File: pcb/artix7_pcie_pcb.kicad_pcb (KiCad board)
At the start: 4 copper layers, 211 parts, among them CON301 BARREL_JACK, J1101 SFP_CONN, J201 PCIe_x1, J801 FX10B-80S/8-SV, J901 JTAG-XILINX-TC, P1201 CONN_02X05, P1202 CONN_02X05, SW1201 SW_PUSH, SW1202 SW_PUSH, SW901 SW_PUSH, U1001 FOX924, U1002 NB3L553, U1003 Si5338C, U301 LTM4622, U302 LTM4622, U303 ADP170, U304 TPS72615, U401 XC7Axxt-FGG484, U501 DDR3-x16, U901 S25FL256SAGNFI

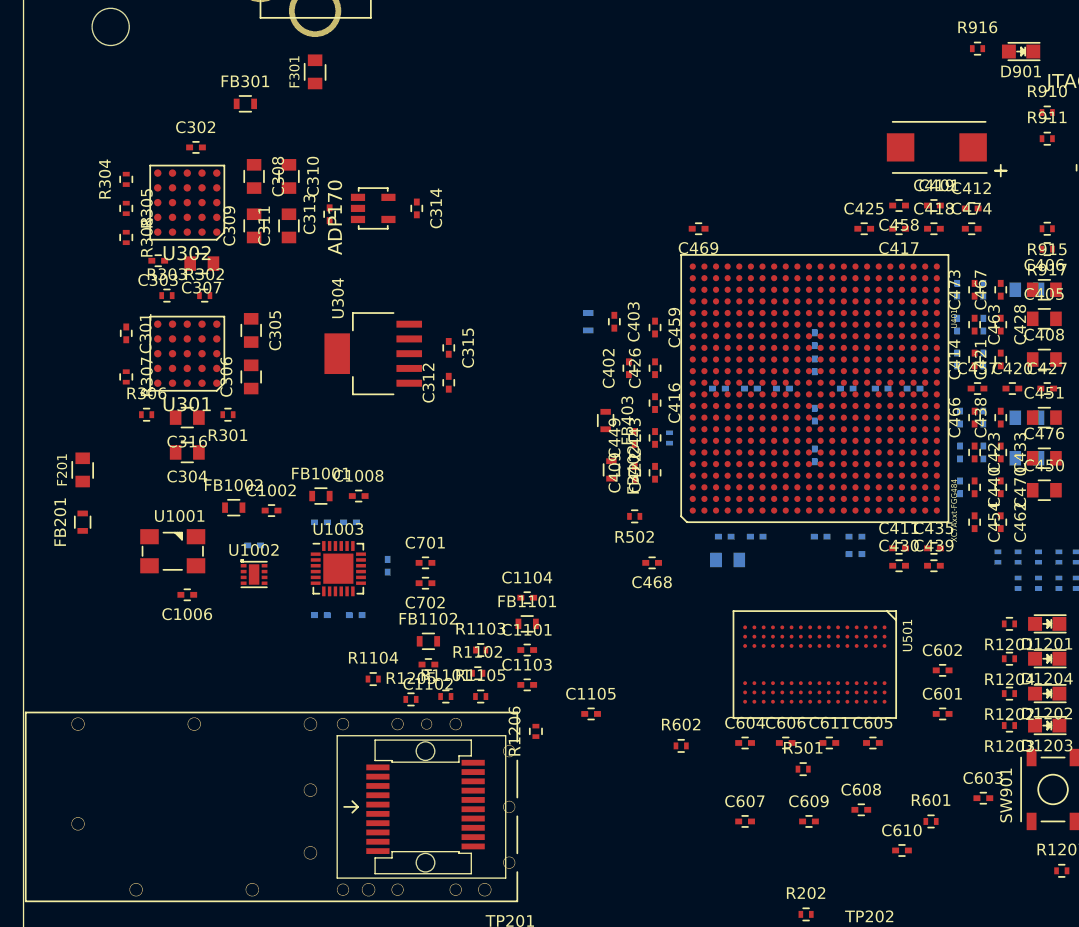
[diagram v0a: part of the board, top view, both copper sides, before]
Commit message: Finished initial component placement
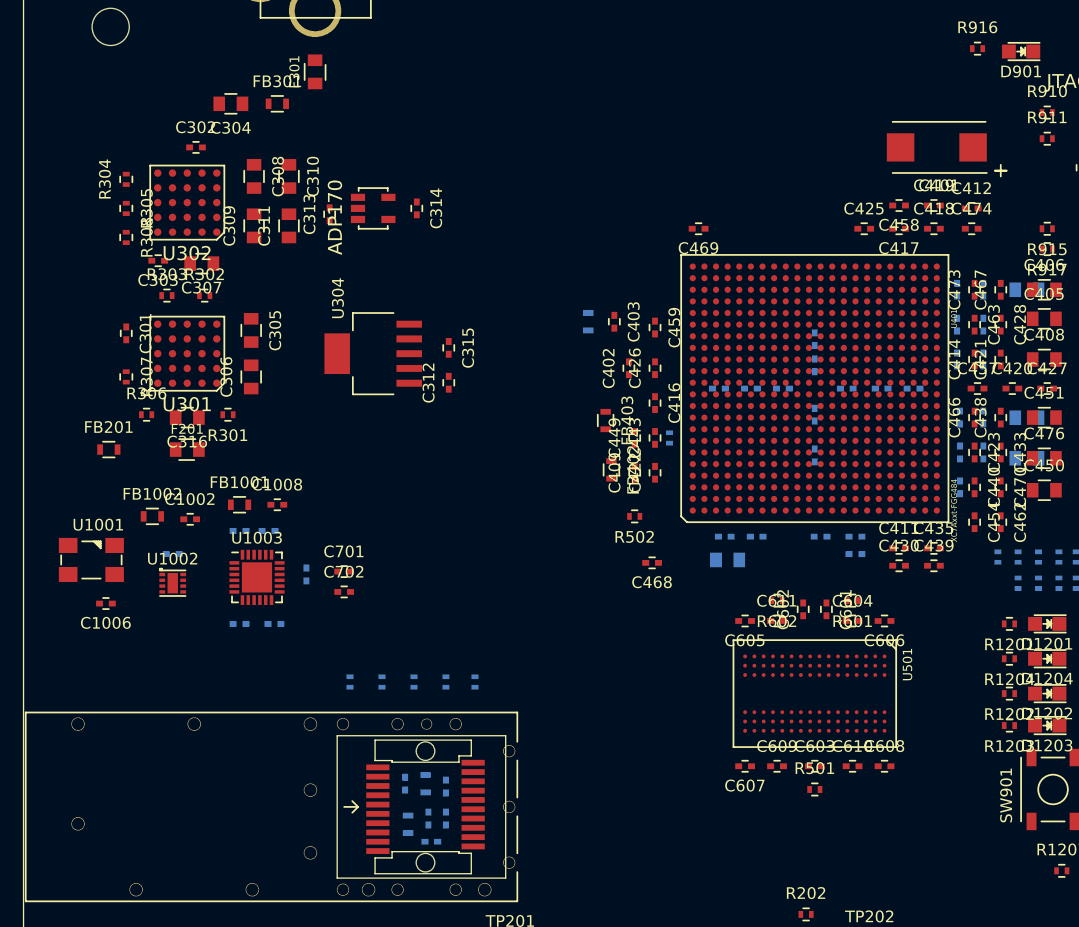
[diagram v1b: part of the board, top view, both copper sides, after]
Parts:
- removed R1205, R1206: R, wbraun_smd:R_0402
- C1101, C1102, C1103, C1104, C1105, FB1101, FB1102, R1101, R1102, R1103, R1104, R1105: moved to B.Cu
- moved C304 30.2 mm to (59.8, 63.0)
- moved C1104 22.6 mm to (77.0, 126.5)
- moved R601 20.2 mm to (113.2, 105.8), turned to 180 degrees
- moved FB1101 20.1 mm to (75.0, 125.0), turned to 90 degrees
- moved C1105 17.1 mm to (74.8, 121.5), turned to 270 degrees
- moved C1101 16.8 mm to (76.8, 124.5), turned to 270 degrees
- moved C605 15.2 mm to (104.0, 107.5), turned to 180 degrees
- moved R602 15.0 mm to (106.8, 105.8), turned to 180 degrees
- moved C603 14.8 mm to (110.0, 120.0)
- moved C604 14.0 mm to (113.2, 107.5)
- moved C606 13.5 mm to (116.0, 107.5), turned to 180 degrees
- moved C1103 13.5 mm to (78.2, 124.5), turned to 270 degrees
- moved C601 13.5 mm to (111.0, 106.5), turned to 270 degrees
- moved C602 13.1 mm to (109.0, 106.5), turned to 90 degrees
- moved FB1102 12.3 mm to (76.5, 121.5), turned to 270 degrees
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
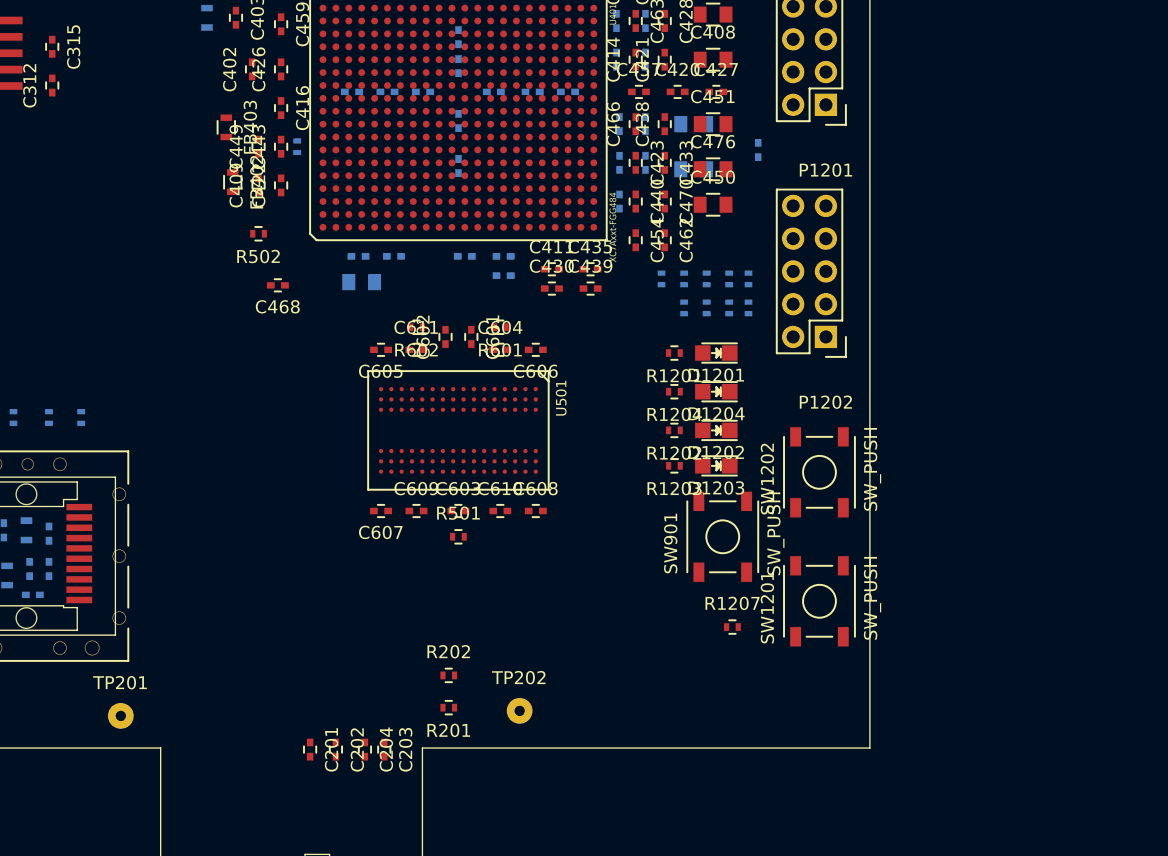
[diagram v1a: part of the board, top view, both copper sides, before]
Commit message: DDR routing test 1
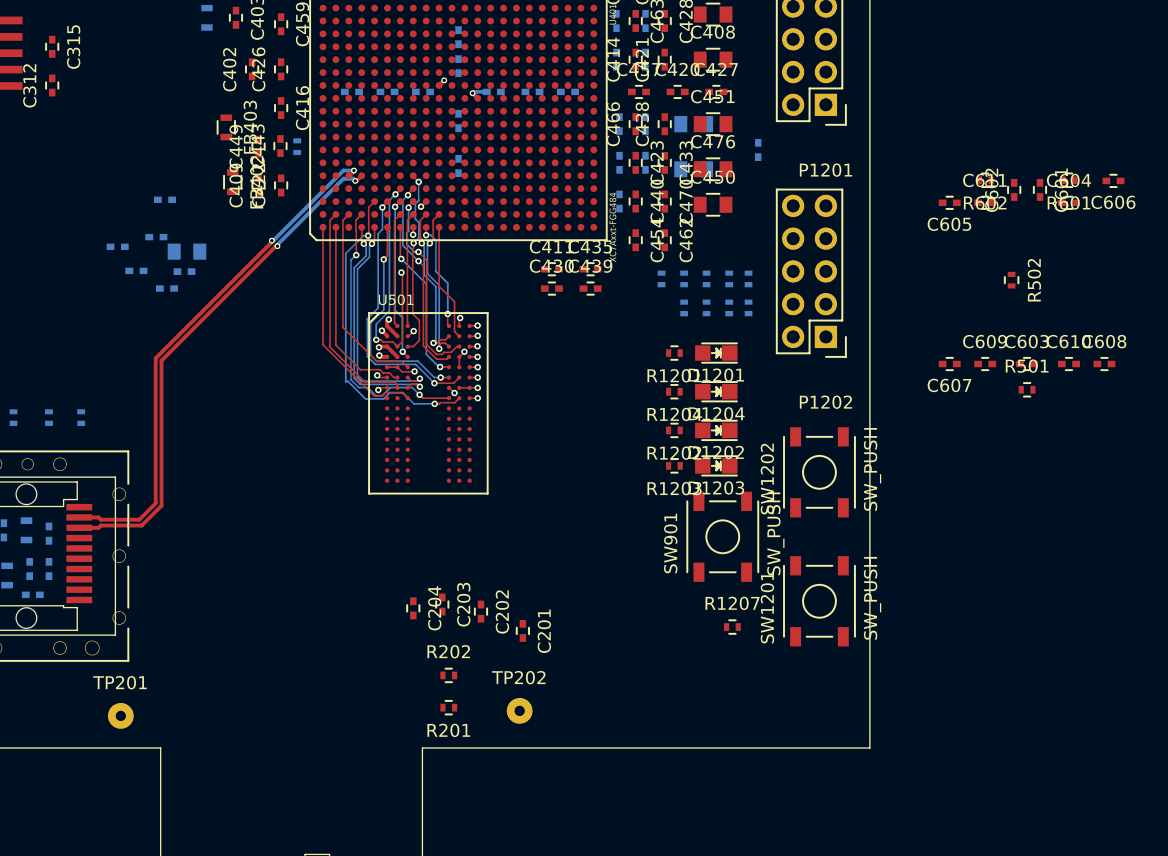
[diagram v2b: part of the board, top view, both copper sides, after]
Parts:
- C468: moved to B.Cu
- moved R502 58.5 mm to (152.9, 102.1), turned to 270 degrees
- moved C606 46.7 mm to (160.8, 94.4)
- moved C601 45.5 mm to (155.1, 95.1)
- moved C602 45.5 mm to (153.1, 95.1)
- moved C603 45.5 mm to (154.1, 108.6)
- moved C604 45.5 mm to (157.3, 96.1)
- moved C605 45.5 mm to (148.1, 96.1)
- moved C607 45.5 mm to (148.1, 108.6)
- moved C608 45.5 mm to (160.1, 108.6)
- moved C609 45.5 mm to (150.8, 108.6)
- moved C610 45.5 mm to (157.3, 108.6)
- moved C611 45.5 mm to (150.8, 96.1)
- moved R501 45.5 mm to (154.1, 110.6)
- moved R601 45.5 mm to (157.3, 94.3)
- moved R602 45.5 mm to (150.8, 94.3)
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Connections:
- U401 pad A1: /DDR3/DDR3_ADDR[11] -> /DDR3/DDR3_DQ[4]
- U401 pad A11: (no net) -> GND
- U401 pad A12: (no net) -> GND
- U401 pad A2: (no net) -> GND
- U401 pad A22: (no net) -> GND
- U401 pad A3: (no net) -> GND
- U401 pad A5: (no net) -> GND
- U401 pad A7: (no net) -> GND
- U401 pad A9: (no net) -> GND
- U401 pad AA12: (no net) -> GND
- U401 pad AA2: (no net) -> GND
- U401 pad AA22: (no net) -> GND
- U401 pad AB19: (no net) -> GND
- U401 pad AB9: (no net) -> GND
- U401 pad B1: /DDR3/DDR3_ADDR[12] -> /DDR3/DDR3_DQ[2]
- U401 pad B12: (no net) -> GND
- U401 pad B19: (no net) -> GND
- U401 pad B2: /DDR3/DDR3_ADDR[9] -> /DDR3/DDR3_DQ[6]
- U401 pad B3: (no net) -> GND
- U401 pad C10: (no net) -> GND
- U401 pad C12: (no net) -> GND
- U401 pad C16: (no net) -> GND
- U401 pad C2: /DDR3/DDR3_ADDR[10] -> /DDR3/DDR3_DQ[0]
- U401 pad C3: (no net) -> GND
- U401 pad C6: (no net) -> GND
- U401 pad D1: /DDR3/DDR3_CK_N -> /DDR3/DDR3_DQS[0]_N
- U401 pad D12: (no net) -> GND
- U401 pad D13: (no net) -> GND
- U401 pad D2: /DDR3/DDR3_ADDR[7] -> /DDR3/DDR3_DQ[7]
- U401 pad D3: (no net) -> GND
- U401 pad D4: (no net) -> GND
- U401 pad D8: (no net) -> GND
- U401 pad E1: /DDR3/DDR3_CK_P -> /DDR3/DDR3_DQS[0]_P
- U401 pad E11: (no net) -> GND
- U401 pad E2: /DDR3/DDR3_ADDR[8] -> Net-(U401-PadE2)
- U401 pad E20: (no net) -> GND
- U401 pad E3: /DDR3/DDR3_ADDR[3] -> /DDR3/DDR3_DQ[5]
- U401 pad E4: (no net) -> GND
- U401 pad E5: (no net) -> GND
- U401 pad E7: (no net) -> GND
- U401 pad E9: (no net) -> GND
- U401 pad F1: /DDR3/DDR3_ADDR[5] -> /DDR3/DDR3_DQ[1]
- U401 pad F11: (no net) -> GND
- U401 pad F17: (no net) -> GND
- U401 pad F3: /DDR3/DDR3_ADDR[4] -> /DDR3/DDR3_DQ[3]
- U401 pad F5: (no net) -> GND
- U401 pad G1: /DDR3/DDR3_ADDR[6] -> /DDR3/DDR3_DM[0]
- U401 pad G10: (no net) -> GND
- U401 pad G12: (no net) -> GND
- U401 pad G14: (no net) -> GND
- U401 pad G2: /DDR3/DDR3_BA[2] -> /DDR3/DDR3_DQ[13]
- U401 pad G3: /DDR3/DDR3_CKE -> /DDR3/DDR3_DM[1]
- U401 pad G4: Net-(U401-PadG4) -> /DDR3/DDR3_DQ[11]
- U401 pad G5: (no net) -> GND
- U401 pad G6: (no net) -> GND
- U401 pad G7: (no net) -> GND
- U401 pad G8: (no net) -> GND
- U401 pad G9: (no net) -> GND
- U401 pad H1: (no net) -> GND
- U401 pad H11: (no net) -> GND
- U401 pad H2: /DDR3/DDR3_ADDR[0] -> /DDR3/DDR3_DQ[15]
- U401 pad H21: (no net) -> GND
- U401 pad H3: /DDR3/DDR3_WE_N -> /DDR3/DDR3_DQ[10]
- U401 pad H4: /DDR3/DDR3_ODT -> /DDR3/DDR3_DQ[8]
- U401 pad H5: /DDR3/DDR3_CAS_N -> /DDR3/DDR3_DQ[9]
- U401 pad H7: (no net) -> GND
- U401 pad H9: (no net) -> GND
- U401 pad J1: /DDR3/DDR3_ADDR[1] -> /DDR3/DDR3_DQ[12]
- U401 pad J10: (no net) -> GND
- U401 pad J12: (no net) -> GND
- U401 pad J18: (no net) -> GND
- U401 pad J2: /DDR3/DDR3_BA[0] -> /DDR3/DDR3_DQS[1]_N
- U401 pad J4: /DDR3/DDR3_DQ[1] -> Net-(U401-PadJ4)
- U401 pad J5: /DDR3/DDR3_RAS_N -> Net-(U401-PadJ5)
- U401 pad J6: /DDR3/DDR3_DQ[6] -> Net-(U401-PadJ6)
- U401 pad J8: (no net) -> GND
- U401 pad K1: /DDR3/DDR3_ADDR[2] -> /DDR3/DDR3_DQ[14]
- U401 pad K11: (no net) -> GND
- U401 pad K15: (no net) -> GND
- U401 pad K2: /DDR3/DDR3_BA[1] -> /DDR3/DDR3_DQS[1]_P
- U401 pad K3: /DDR3/DDR3_DQ[3] -> Net-(U401-PadK3)
- U401 pad K4: /DDR3/DDR3_DQ[0] -> Net-(U401-PadK4)
- U401 pad K5: (no net) -> GND
- U401 pad K6: /DDR3/DDR3_DQ[5] -> Net-(U401-PadK6)
- U401 pad K7: (no net) -> GND
- U401 pad K9: (no net) -> GND
- U401 pad L1: /DDR3/DDR3_DQS[0]_N -> Net-(U401-PadL1)
- U401 pad L2: (no net) -> GND
- U401 pad L22: (no net) -> GND
- U401 pad L3: /DDR3/DDR3_DQ[2] -> Net-(U401-PadL3)
- U401 pad L4: /DDR3/DDR3_RESET_N -> Net-(U401-PadL4)
- U401 pad L5: /DDR3/DDR3_DQ[7] -> Net-(U401-PadL5)
- U401 pad L8: (no net) -> GND
- U401 pad M1: /DDR3/DDR3_DQS[0]_P -> Net-(U401-PadM1)
- U401 pad M11: (no net) -> GND
- U401 pad M19: (no net) -> GND
- U401 pad M2: /DDR3/DDR3_DQ[4] -> Net-(U401-PadM2)
- U401 pad M3: /DDR3/DDR3_DM[0] -> Net-(U401-PadM3)
- U401 pad M5: /DDR3/DDR3_DQ[14] -> Net-(U401-PadM5)
- U401 pad M6: /DDR3/DDR3_DQ[13] -> Net-(U401-PadM6)
- U401 pad M7: (no net) -> GND
- U401 pad N16: (no net) -> GND
- U401 pad N2: /DDR3/DDR3_DQ[12] -> Net-(U401-PadN2)
- U401 pad N3: /DDR3/DDR3_DQ[8] -> Net-(U401-PadN3)
- U401 pad N4: /DDR3/DDR3_DM[1] -> Net-(U401-PadN4)
- U401 pad N6: (no net) -> GND
- U401 pad N8: (no net) -> GND
- U401 pad P1: /DDR3/DDR3_DQ[10] -> Net-(U401-PadP1)
- U401 pad P11: (no net) -> GND
- U401 pad P13: (no net) -> GND
- U401 pad P2: /DDR3/DDR3_DQ[11] -> Net-(U401-PadP2)
- U401 pad P3: (no net) -> GND
- U401 pad P4: /DDR3/DDR3_DQS[1]_N -> Net-(U401-PadP4)
- U401 pad P5: /DDR3/DDR3_DQS[1]_P -> Net-(U401-PadP5)
- U401 pad P6: /DDR3/DDR3_DQ[15] -> Net-(U401-PadP6)
- U401 pad P7: (no net) -> GND
- U401 pad P9: (no net) -> GND
- U401 pad R1: /DDR3/DDR3_DQ[9] -> Net-(U401-PadR1)
- U401 pad R10: (no net) -> GND
- U401 pad R12: (no net) -> GND
- U401 pad R20: (no net) -> GND
- U401 pad R8: (no net) -> GND
- U401 pad T11: (no net) -> GND
- U401 pad T17: (no net) -> GND
- U401 pad T7: (no net) -> GND
- U401 pad T9: (no net) -> GND
- U401 pad U14: (no net) -> GND
- U401 pad U4: (no net) -> GND
- U401 pad V1: (no net) -> GND
- U401 pad V11: (no net) -> GND
- U401 pad V21: (no net) -> GND
- U401 pad W18: (no net) -> GND
- U401 pad W8: (no net) -> GND
- U401 pad Y15: (no net) -> GND
- U401 pad Y5: (no net) -> GND
- U501 pad E9: (no net) -> +1V5
- U501 pad H2: (no net) -> +1V5
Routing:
- net /FPGA Transceivers/SFP_TX_P: track 0.00 -> 40.0 mm, vias 0 -> 2
- net /FPGA Transceivers/SFP_TX_N: track 0.00 -> 39.8 mm, vias 0 -> 2
- net /DDR3/DDR3_DQ[5]: track 0.00 -> 25.2 mm, vias 0 -> 2
- net /DDR3/DDR3_DQ[7]: track 0.00 -> 21.9 mm, vias 0 -> 2
- net /DDR3/DDR3_DQ[3]: track 0.00 -> 20.8 mm, vias 0 -> 2
- net /DDR3/DDR3_DQ[11]: track 0.00 -> 20.3 mm, vias 0 -> 3
- net /DDR3/DDR3_DQS[0]_N: track 0.00 -> 18.7 mm, vias 0 -> 2
- net /DDR3/DDR3_DQS[0]_P: track 0.00 -> 18.3 mm, vias 0 -> 2
- net /DDR3/DDR3_DQ[4]: track 0.00 -> 17.6 mm
- net /DDR3/DDR3_DQ[1]: track 0.00 -> 17.3 mm, vias 0 -> 2
- net /DDR3/DDR3_DQ[6]: track 0.00 -> 17.2 mm
- net /DDR3/DDR3_DQ[8]: track 0.00 -> 15.7 mm, vias 0 -> 2
- net /DDR3/DDR3_DQ[0]: track 0.00 -> 15.3 mm
- net /DDR3/DDR3_DQ[10]: track 0.00 -> 15.2 mm, vias 0 -> 2
- net /DDR3/DDR3_DQ[2]: track 0.00 -> 14.9 mm
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- added copper zone on In2.Cu, net +1V0
- added copper zone on In2.Cu, net +1V8
- added copper zone on In1.Cu, net GND
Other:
- net class Default: via_dia 0.4572 -> 0.5
- rule via_min_size: 0.457 -> 0.5

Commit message: Finished most of the routing, removed DDR-3
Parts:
- removed C312, C315: 4.7uF, wbraun_smd:C_0402
- removed C601, C602: 10nF, wbraun_smd:C_0402
- removed C603, C604, C605, C606, C607, C608, C609, C610, C611: 0.47uF, wbraun_smd:C_0402
- removed R501: 240, wbraun_smd:R_0402
- removed R502: 100, wbraun_smd:R_0402
- removed R601, R602: 1K, wbraun_smd:R_0402
- removed U304: TPS72615, wbraun_smd:SOT223-5
- removed U501: DDR3-x16, wbraun_smd:FBGA-96-DDR3-SDRAM
- added R1001: R, wbraun_smd:R_0402, F.Cu at (80.7, 56.5)
- added R1002: R, wbraun_smd:R_0402, F.Cu at (78.9, 56.5)
- C1001, C1003, C1004, C1005, C1007, C1009, C472, C477, R901, R902, R907, R908, R912, R913, R918, R919: moved to F.Cu
- C313, C314, C402, C410, C411, C412, C413, C415, C417, C418, C419, C420, C421, C423, C424, C425, C426, C428, C429, C430, C432, C433, C434, C435, C436, C438, C439, C440, C444, C445, C446, C447, C453, C454, C455, C456, C458, C459, C460, C461, C462, C463, C464, C465, C466, C467, C468, C469, C470, C471, C473, C474, C475: footprint wbraun_smd:C_0402 -> wbraun_smd:0402_in_grid
- C403, C409, C414, C416, C422, C427, C443, C449, C457: footprint wbraun_smd:C_0402 -> wbraun_smd:0402_in_grid; moved to B.Cu
- C407, C431, C437, C441, C442, C448: footprint wbraun_smd:C_0402 -> wbraun_smd:0402_in_grid; moved to F.Cu
- J901: footprint wbraun_smd:TC2030-IDC-FP -> wbraun_smd:TC2030-IDC-NL
- moved J201 179.6 mm to (-79.6, 169.3)
- moved C423 118.2 mm to (227.8, 37.0)
- moved C433 118.2 mm to (230.1, 37.0)
- moved C438 118.2 mm to (230.1, 34.0)
- moved C440 118.2 mm to (227.8, 40.0)
- moved C454 118.2 mm to (227.8, 43.0)
- moved C462 118.2 mm to (230.1, 43.0)
- moved C466 118.2 mm to (227.8, 34.0)
- moved C470 118.2 mm to (230.1, 40.0)
- moved C412 98.8 mm to (215.1, 35.0)
- moved C417 98.8 mm to (208.9, 36.8)
- moved C418 98.8 mm to (211.9, 36.8)
- moved C419 98.8 mm to (211.9, 34.8)
- moved C425 98.8 mm to (205.9, 36.8)
- moved C458 98.8 mm to (208.9, 34.8)
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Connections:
- C1008 pad 1: Net-(C1008-Pad1) -> /Clocking/CLOCK_GEN_POWER
- C1008 pad 2: Net-(C1008-Pad2) -> GND
- C432 pad 2: Net-(C432-Pad2) -> GND
- C452 pad 1: +1V5 -> +3V3
- C456 pad 1: +1V5 -> +3V3
- C460 pad 1: +1V5 -> +3V3
- C464 pad 1: +1V5 -> +3V3
- C468 pad 1: +1V5 -> +3V3
- C471 pad 1: +1V5 -> +3V3
- C475 pad 1: +1V5 -> +3V3
- F301 pad 1: Net-(F301-Pad1) -> +12V
- F301 pad 2: Net-(CON301-Pad1) -> Net-(F301-Pad2)
- FB301 pad 1: +12V -> Net-(F301-Pad2)
- FB301 pad 2: Net-(F301-Pad1) -> Net-(CON301-Pad1)
- J1101 pad 2: /User IO/SFP_TX_FAULT -> /MyriadRF IO/SFP_TX_FAULT
- J1101 pad 3: /SFP/TX_DISABLE -> /MyriadRF IO/SFP_TX_DISABLE
- J1101 pad 4: /SFP/SFP_SDA -> /MyriadRF IO/SFP_SDA
- J1101 pad 5: /SFP/SFP_SCL -> /MyriadRF IO/SFP_SCL
- J1101 pad 6: /SFP/SFP_DETECT -> /MyriadRF IO/SFP_DETECT
- J1101 pad 7: /SFP/RATE_SEL -> /MyriadRF IO/SFP_RATE_SEL
- R1101 pad 2: /SFP/SFP_SDA -> /MyriadRF IO/SFP_SDA
- R1102 pad 2: /SFP/SFP_SCL -> /MyriadRF IO/SFP_SCL
- R1103 pad 2: /SFP/SFP_DETECT -> /MyriadRF IO/SFP_DETECT
- R1105 pad 2: /User IO/SFP_TX_FAULT -> /MyriadRF IO/SFP_TX_FAULT
- R201 pad 1: /User IO/PCIE_PERST -> /PCIe Connector/PERST#
- U401 pad A1: /DDR3/DDR3_DQ[4] -> (no net)
- U401 pad A10: Net-(U401-PadA10) -> /FPGA Transceivers/SFP_RX_P
- U401 pad A13: (no net) -> /MyriadRF IO/SFP_TX_DISABLE
- U401 pad A14: (no net) -> /MyriadRF IO/SFP_SCL
- U401 pad A15: (no net) -> /MyriadRF IO/SFP_RATE_SEL
- U401 pad A16: (no net) -> /Clocking/CLK_SDA
- U401 pad A18: (no net) -> Net-(U401-PadA18)
- U401 pad A19: (no net) -> Net-(U401-PadA19)
- U401 pad A20: (no net) -> /MyriadRF IO/TXEN
- U401 pad A21: (no net) -> /MyriadRF IO/RXEN
- U401 pad A4: /FPGA Transceivers/PCIE_TX0_N -> /FPGA Transceivers/PCIE_TX0_P
- U401 pad A6: Net-(U401-PadA6) -> /FPGA Transceivers/SFP_TX_N
- U401 pad A8: /FPGA Transceivers/PCIE_RX0_N -> /FPGA Transceivers/PCIE_RX0_P
- U401 pad AA6: /SFP/LOS -> Net-(U401-PadAA6)
- U401 pad AB6: /SFP/SFP_SCL -> Net-(U401-PadAB6)
- U401 pad AB7: /SFP/SFP_SDA -> Net-(U401-PadAB7)
- U401 pad B1: /DDR3/DDR3_DQ[2] -> (no net)
- U401 pad B10: Net-(U401-PadB10) -> /FPGA Transceivers/SFP_RX_N
- U401 pad B13: (no net) -> /MyriadRF IO/SFP_TX_FAULT
- U401 pad B15: (no net) -> /SFP/LOS
- U401 pad B16: (no net) -> /Clocking/CLK_SCL
- U401 pad B17: (no net) -> /Clocking/FPGA_CLK
- U401 pad B18: (no net) -> Net-(U401-PadB18)
- U401 pad B2: /DDR3/DDR3_DQ[6] -> (no net)
- U401 pad B20: (no net) -> /MyriadRF IO/SPI_NCSO
- U401 pad B21: (no net) -> /MyriadRF IO/SPI_CLK
- U401 pad B22: (no net) -> /MyriadRF IO/GPIO2
- U401 pad B4: /FPGA Transceivers/PCIE_TX0_P -> /FPGA Transceivers/PCIE_TX0_N
- U401 pad B6: Net-(U401-PadB6) -> /FPGA Transceivers/SFP_TX_P
- U401 pad B8: /FPGA Transceivers/PCIE_RX0_P -> /FPGA Transceivers/PCIE_RX0_N
- U401 pad C1: +1V5 -> +3V3
- U401 pad C11: /FPGA Transceivers/SFP_RX_N -> Net-(U401-PadC11)
- U401 pad C13: (no net) -> /MyriadRF IO/SFP_SDA
- U401 pad C14: (no net) -> /MyriadRF IO/SFP_DETECT
- U401 pad C15: (no net) -> Net-(U401-PadC15)
- U401 pad C17: (no net) -> Net-(U401-PadC17)
- U401 pad C18: (no net) -> /Clocking/RX_CLK_FPGA
- U401 pad C19: (no net) -> /MyriadRF IO/SPI_MISO
- U401 pad C2: /DDR3/DDR3_DQ[0] -> (no net)
- U401 pad C20: (no net) -> /MyriadRF IO/GPIO1
- U401 pad C22: (no net) -> /MyriadRF IO/SPI_MOSI
- U401 pad C5: /FPGA Transceivers/SFP_TX_N -> Net-(U401-PadC5)
- U401 pad D1: /DDR3/DDR3_DQS[0]_N -> (no net)
- U401 pad D11: /FPGA Transceivers/SFP_RX_P -> Net-(U401-PadD11)
- U401 pad D14: (no net) -> Net-(U401-PadD14)
- U401 pad D15: (no net) -> Net-(U401-PadD15)
- U401 pad D16: (no net) -> Net-(U401-PadD16)
- U401 pad D17: (no net) -> /Clocking/TX_CLK_FPGA
- U401 pad D19: (no net) -> /MyriadRF IO/RESET
- U401 pad D2: /DDR3/DDR3_DQ[7] -> (no net)
- U401 pad D20: (no net) -> /MyriadRF IO/GPIO0
- U401 pad D21: (no net) -> /MyriadRF IO/RXD11
- U401 pad D22: (no net) -> /MyriadRF IO/RXD10
- U401 pad D5: /FPGA Transceivers/SFP_TX_P -> Net-(U401-PadD5)
- U401 pad E1: /DDR3/DDR3_DQS[0]_P -> (no net)
- U401 pad E10: /FPGA Transceivers/SFP_CLK_C_N -> /FPGA Transceivers/SFP_CLK_C_P
- U401 pad E13: (no net) -> Net-(U401-PadE13)
- U401 pad E14: (no net) -> Net-(U401-PadE14)
- U401 pad E16: (no net) -> Net-(U401-PadE16)
- U401 pad E17: (no net) -> Net-(U401-PadE17)
- U401 pad E18: (no net) -> Net-(U401-PadE18)
- U401 pad E19: (no net) -> /MyriadRF IO/RXD9
- U401 pad E2: Net-(U401-PadE2) -> (no net)
- U401 pad E21: (no net) -> /MyriadRF IO/RXD8
- U401 pad E22: (no net) -> /MyriadRF IO/RXD7
- U401 pad E3: /DDR3/DDR3_DQ[5] -> (no net)
- U401 pad F1: /DDR3/DDR3_DQ[1] -> (no net)
- U401 pad F10: /FPGA Transceivers/SFP_CLK_C_P -> /FPGA Transceivers/SFP_CLK_C_N
- U401 pad F13: (no net) -> Net-(U401-PadF13)
- U401 pad F14: (no net) -> Net-(U401-PadF14)
- U401 pad F15: (no net) -> Net-(U401-PadF15)
- U401 pad F16: (no net) -> Net-(U401-PadF16)
- U401 pad F18: (no net) -> Net-(U401-PadF18)
- U401 pad F19: (no net) -> /MyriadRF IO/RXD6
- U401 pad F2: +1V5 -> +3V3
- U401 pad F20: (no net) -> /MyriadRF IO/RXD5
- U401 pad F21: (no net) -> /MyriadRF IO/RXD4
- U401 pad F3: /DDR3/DDR3_DQ[3] -> (no net)
- U401 pad F4: Net-(U401-PadF4) -> (no net)
- U401 pad G1: /DDR3/DDR3_DM[0] -> (no net)
- U401 pad G2: /DDR3/DDR3_DQ[13] -> (no net)
- U401 pad G20: /MyriadRF IO/TXD5 -> /MyriadRF IO/RXD3
- U401 pad G21: (no net) -> /MyriadRF IO/RXD2
- U401 pad G22: (no net) -> /MyriadRF IO/RXD1
- U401 pad G3: /DDR3/DDR3_DM[1] -> (no net)
- U401 pad G4: /DDR3/DDR3_DQ[11] -> (no net)
- U401 pad H15: /MyriadRF IO/TXIQSEL -> Net-(U401-PadH15)
- U401 pad H17: /MyriadRF IO/TXD0 -> Net-(U401-PadH17)
- U401 pad H18: /MyriadRF IO/TXD1 -> Net-(U401-PadH18)
- U401 pad H19: Net-(U401-PadH19) -> /MyriadRF IO/RXD0
- U401 pad H2: /DDR3/DDR3_DQ[15] -> (no net)
- U401 pad H20: /MyriadRF IO/TXD4 -> /MyriadRF IO/RXIQSEL
- U401 pad H22: /MyriadRF IO/TXD3 -> /MyriadRF IO/TXD11
- U401 pad H3: /DDR3/DDR3_DQ[10] -> (no net)
- U401 pad H4: /DDR3/DDR3_DQ[8] -> (no net)
- U401 pad H5: /DDR3/DDR3_DQ[9] -> (no net)
- U401 pad H6: +1V5 -> +3V3
- U401 pad J1: /DDR3/DDR3_DQ[12] -> (no net)
- U401 pad J17: /MyriadRF IO/SPI_MISO -> Net-(U401-PadJ17)
- U401 pad J19: /Clocking/TX_CLK_FPGA -> /MyriadRF IO/TXD10
- U401 pad J2: /DDR3/DDR3_DQS[1]_N -> (no net)
- U401 pad J20: /MyriadRF IO/TXD10 -> /MyriadRF IO/TXD9
- U401 pad J21: /MyriadRF IO/TXD11 -> /MyriadRF IO/TXD8
- U401 pad J22: /MyriadRF IO/TXD2 -> /MyriadRF IO/TXD7
- U401 pad J3: +1V5 -> +3V3
- U401 pad J4: Net-(U401-PadJ4) -> (no net)
- U401 pad J5: Net-(U401-PadJ5) -> (no net)
- U401 pad J6: Net-(U401-PadJ6) -> (no net)
- U401 pad K1: /DDR3/DDR3_DQ[14] -> (no net)
- U401 pad K13: /MyriadRF IO/RXD9 -> Net-(U401-PadK13)
- U401 pad K14: /MyriadRF IO/RXD10 -> Net-(U401-PadK14)
- U401 pad K16: /MyriadRF IO/GPIO1 -> Net-(U401-PadK16)
- U401 pad K17: /MyriadRF IO/SPI_MOSI -> Net-(U401-PadK17)
- U401 pad K18: /Clocking/RX_CLK_FPGA -> Net-(U401-PadK18)
- U401 pad K19: Net-(U401-PadK19) -> /MyriadRF IO/TXD6
- U401 pad K2: /DDR3/DDR3_DQS[1]_P -> (no net)
- U401 pad K21: /MyriadRF IO/TXD6 -> /MyriadRF IO/TXD5
- U401 pad K22: /MyriadRF IO/TXD7 -> /MyriadRF IO/TXD4
- U401 pad K3: Net-(U401-PadK3) -> (no net)
- U401 pad K4: Net-(U401-PadK4) -> (no net)
- U401 pad K6: Net-(U401-PadK6) -> (no net)
- U401 pad L1: Net-(U401-PadL1) -> (no net)
- U401 pad L12: /FPGA Config/QSPI_SCK -> /FPGA Config/QSPI_CLK
- U401 pad L13: /MyriadRF IO/RESET -> Net-(U401-PadL13)
- U401 pad L14: /MyriadRF IO/SPI_CLK -> Net-(U401-PadL14)
- U401 pad L15: /MyriadRF IO/SPI_NCSO -> Net-(U401-PadL15)
- U401 pad L16: /MyriadRF IO/GPIO0 -> Net-(U401-PadL16)
- U401 pad L18: /MyriadRF IO/RXD4 -> Net-(U401-PadL18)
- U401 pad L19: /MyriadRF IO/RXIQSEL -> /MyriadRF IO/TXD3
- U401 pad L20: /MyriadRF IO/RXD0 -> /MyriadRF IO/TXD2
- U401 pad L21: /MyriadRF IO/TXD9 -> /MyriadRF IO/TXD1
- U401 pad L3: Net-(U401-PadL3) -> (no net)
- U401 pad L4: Net-(U401-PadL4) -> (no net)
- U401 pad L5: Net-(U401-PadL5) -> (no net)
- U401 pad L6: Net-(U401-PadL6) -> (no net)
- U401 pad M1: Net-(U401-PadM1) -> (no net)
- U401 pad M13: /MyriadRF IO/RXD11 -> Net-(U401-PadM13)
- U401 pad M15: /MyriadRF IO/GPIO2 -> Net-(U401-PadM15)
- U401 pad M16: /MyriadRF IO/TXEN -> Net-(U401-PadM16)
- U401 pad M17: /MyriadRF IO/RXEN -> Net-(U401-PadM17)
- U401 pad M18: /MyriadRF IO/RXD3 -> Net-(U401-PadM18)
- U401 pad M2: Net-(U401-PadM2) -> (no net)
- U401 pad M20: /MyriadRF IO/RXD8 -> Net-(U401-PadM20)
- U401 pad M21: /MyriadRF IO/TXD8 -> Net-(U401-PadM21)
- U401 pad M22: /MyriadRF IO/RXD2 -> /MyriadRF IO/TXD0
- U401 pad M3: Net-(U401-PadM3) -> (no net)
- U401 pad M4: +1V5 -> +3V3
- U401 pad M5: Net-(U401-PadM5) -> (no net)
- U401 pad M6: Net-(U401-PadM6) -> (no net)
- U401 pad N1: +1V5 -> +3V3
- U401 pad N18: /MyriadRF IO/RXD5 -> Net-(U401-PadN18)
- U401 pad N19: /MyriadRF IO/RXD6 -> Net-(U401-PadN19)
- U401 pad N2: Net-(U401-PadN2) -> (no net)
- U401 pad N20: /MyriadRF IO/RXD7 -> Net-(U401-PadN20)
- U401 pad N22: /MyriadRF IO/RXD1 -> /MyriadRF IO/TXIQSEL
- U401 pad N3: Net-(U401-PadN3) -> (no net)
- U401 pad N4: Net-(U401-PadN4) -> (no net)
- U401 pad N5: Net-(U401-PadN5) -> (no net)
- U401 pad P1: Net-(U401-PadP1) -> (no net)
- U401 pad P2: Net-(U401-PadP2) -> (no net)
- U401 pad P4: Net-(U401-PadP4) -> (no net)
- U401 pad P5: Net-(U401-PadP5) -> (no net)
- U401 pad P6: Net-(U401-PadP6) -> (no net)
- U401 pad R1: Net-(U401-PadR1) -> (no net)
- U401 pad V7: /User IO/SFP_TX_FAULT -> Net-(U401-PadV7)
- U401 pad V9: /User IO/PCIE_PERST -> Net-(U401-PadV9)
- U401 pad W19: /Clocking/FPGA_CLK -> /FPGA Config/FPGA_CLK
- U401 pad W7: /SFP/SFP_DETECT -> Net-(U401-PadW7)
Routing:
- net GND: track 10.2 -> 185.2 mm, vias 11 -> 178
- net /SFP/LOS: track 0.00 -> 79.3 mm, vias 0 -> 2
- net /MyriadRF IO/SFP_RATE_SEL: track 0.00 -> 72.8 mm, vias 0 -> 2
- net (no net): track 0.00 -> 71.1 mm
- net /MyriadRF IO/SFP_DETECT: track 0.00 -> 70.4 mm, vias 0 -> 2
- net /FPGA Transceivers/PCIE_RX0_N: track 0.00 -> 67.8 mm
- net /FPGA Transceivers/PCIE_RX0_P: track 0.00 -> 67.0 mm
- net +3V3: track 0.00 -> 66.5 mm, vias 0 -> 61
- net /MyriadRF IO/SFP_SCL: track 0.00 -> 65.2 mm, vias 0 -> 2
- net /Clocking/CLK_SDA: track 0.00 -> 62.3 mm, vias 0 -> 3
- net /MyriadRF IO/SFP_SDA: track 0.00 -> 61.2 mm, vias 0 -> 2
- net /MyriadRF IO/SFP_TX_DISABLE: track 0.00 -> 58.9 mm, vias 0 -> 2
- net /MyriadRF IO/SFP_TX_FAULT: track 0.00 -> 58.0 mm, vias 0 -> 2
- net /FPGA Transceivers/SFP_CLK_C_N: track 0.00 -> 50.2 mm, vias 0 -> 2
- net /Clocking/RX_CLK_FPGA: track 0.00 -> 49.8 mm, vias 0 -> 2
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- added copper zone on In2.Cu, net +12V
- added copper zone on F.Cu, net +1V0
- added copper zone on F.Cu, net +1V8
- added copper zone on In2.Cu, net +3V3
- added copper zone on In2.Cu, net +5V
- added copper zone on In2.Cu, net /Clocking/CLOCK_GEN_POWER
- added copper zone on In2.Cu, net /Clocking/OSC_POWER
- added copper zone on In2.Cu, net /FPGA Power/MGTAVCC
- added copper zone on B.Cu, net GND
- added copper zone on In2.Cu, net GND
- added copper zone on In2.Cu, net MGTAVTT
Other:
- board outline added: 100 x 115.2 mm
- rule pad_to_mask_clearance: 0.2 -> 0.0635
- board text added: "100 ohm diff: 0.15mm width, 0.15mm spacing 50 ohm SE: 0.35mm"
